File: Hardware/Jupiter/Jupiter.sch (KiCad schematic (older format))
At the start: 32 parts

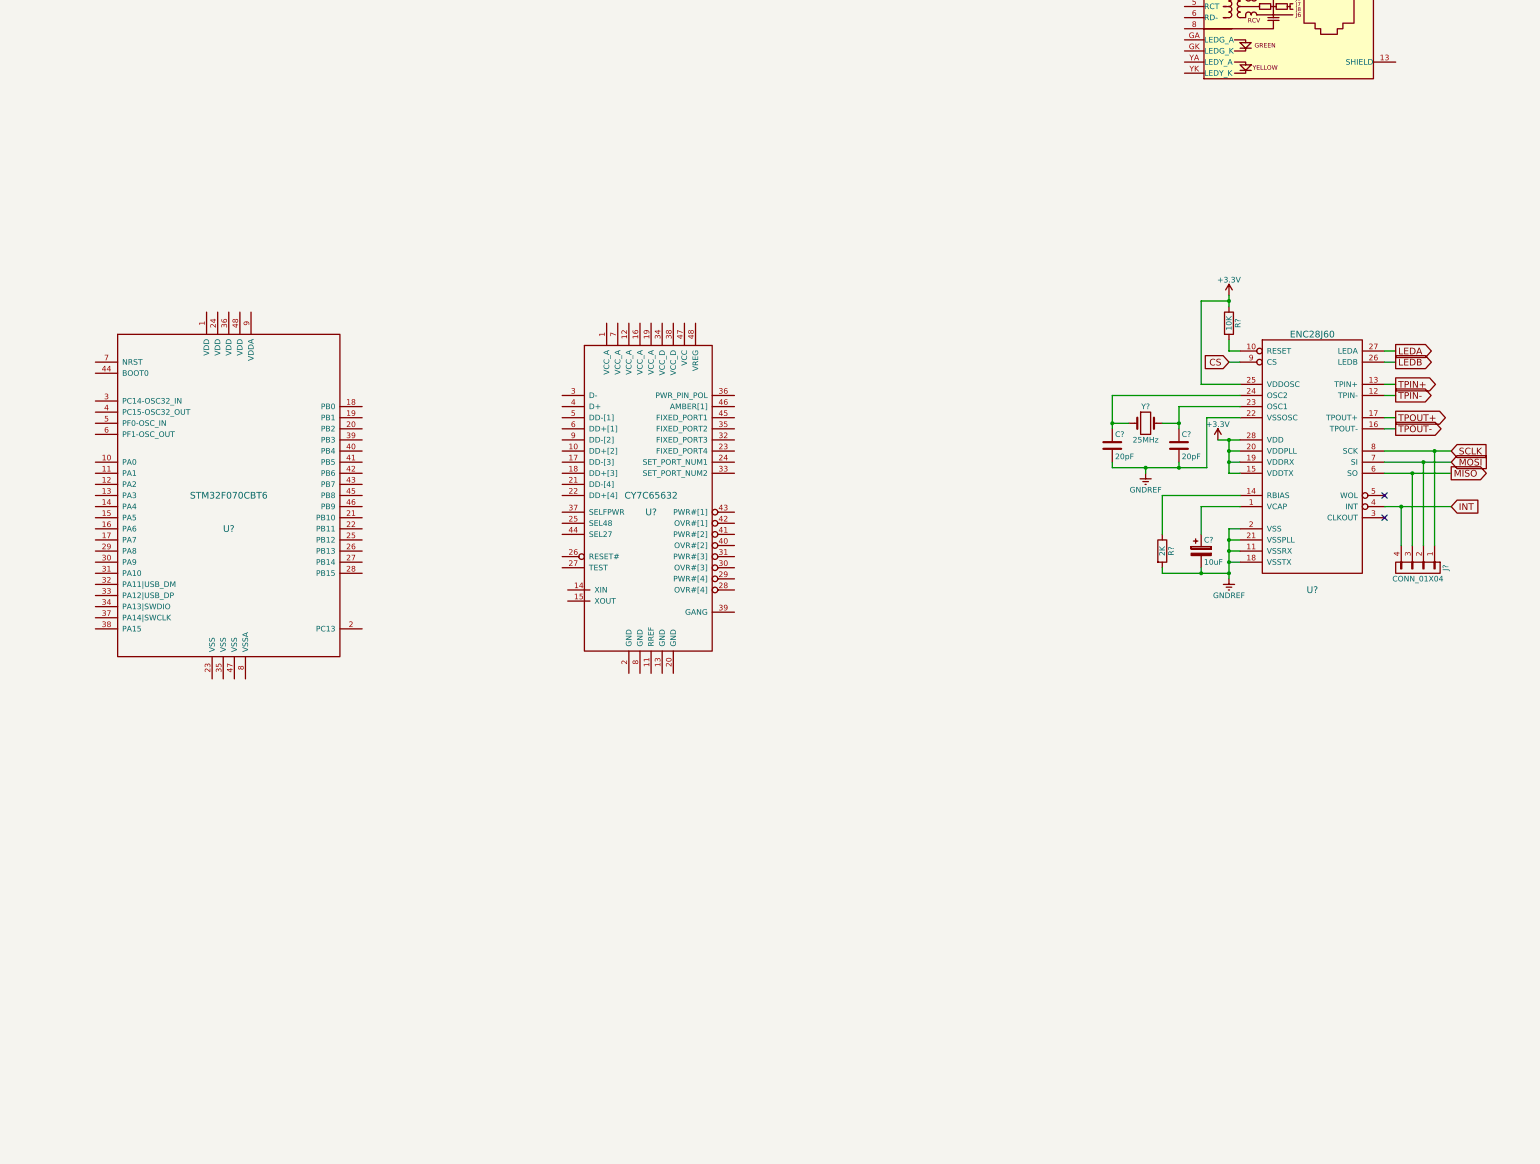
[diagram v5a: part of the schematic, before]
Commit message: USB additions.
1) Add external facing USB ports.
2) Add USB power control circuitry, cuts power to downstream USB in event of shorted pins (i.e., dodgey cabling).
3) Start filling out details for Cypress USB hub.
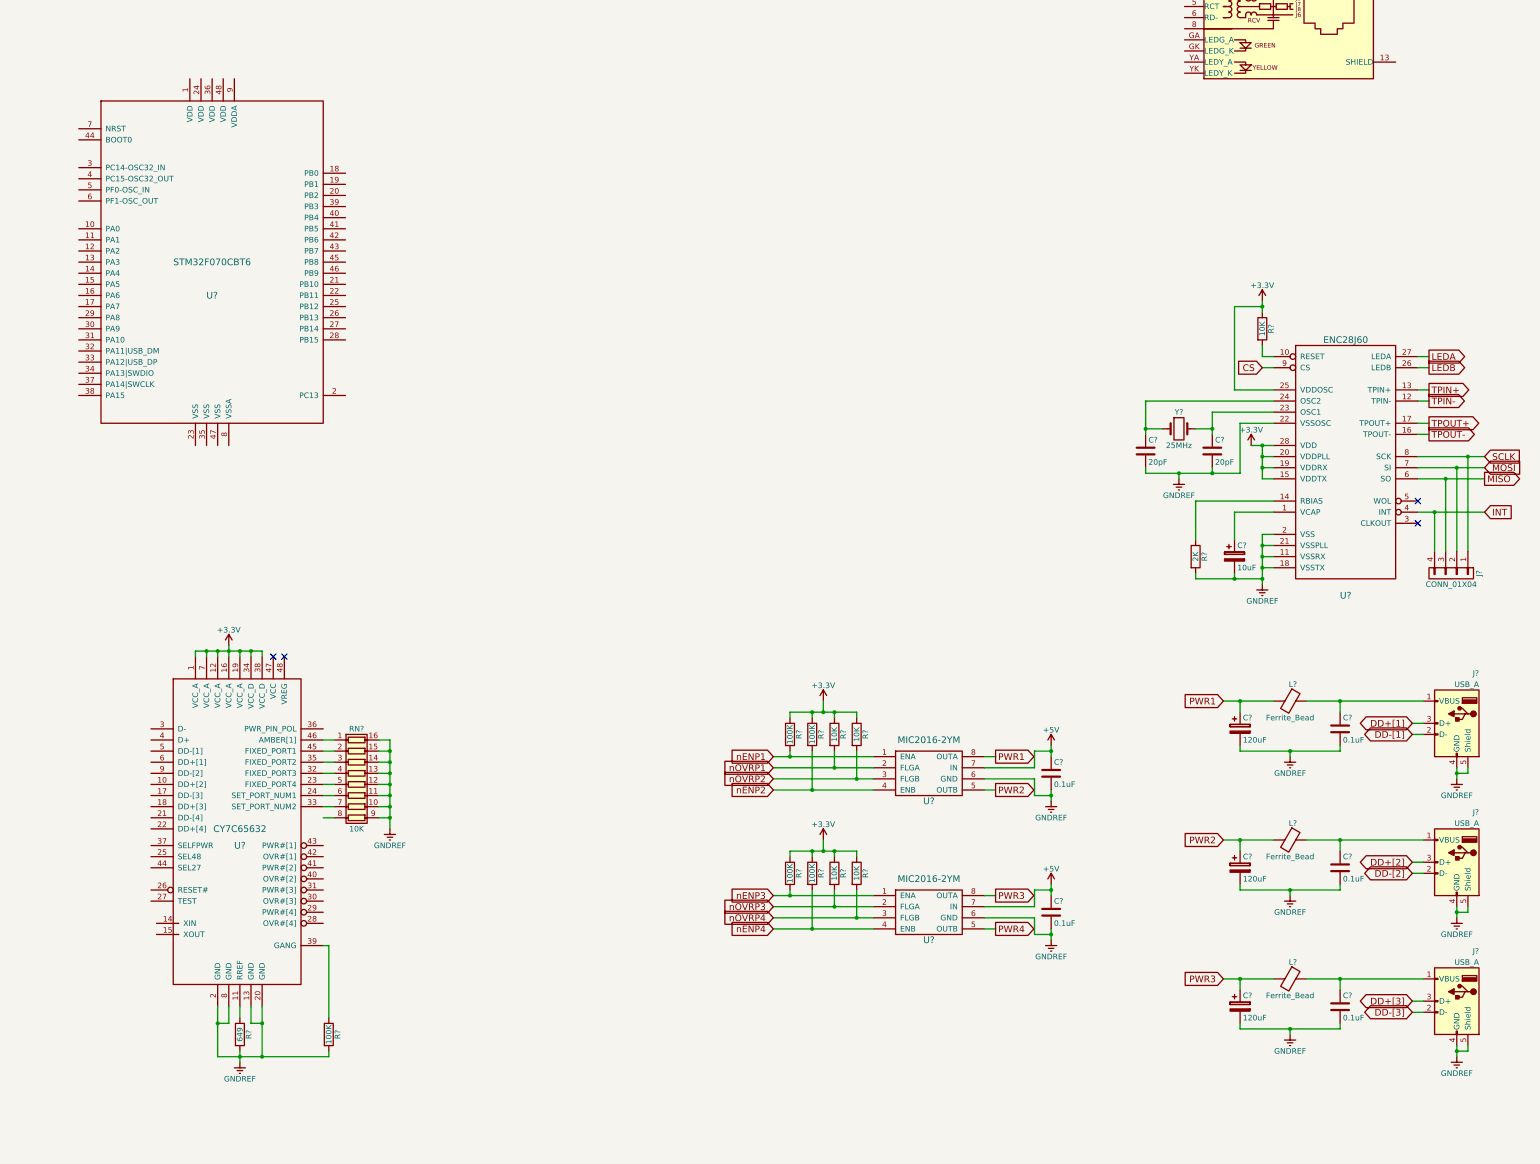
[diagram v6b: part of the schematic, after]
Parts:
- added C? (x5): 0.1uF, symbol C
- added C? (x3): 120uF, symbol CP
- added J? (x3): USB_A, symbol USB_A
- added L? (x3): Ferrite_Bead, symbol Ferrite_Bead
- added R? (x4): 10K, symbol R
- added R? (x5): 100K, symbol R
- added R?: 649, symbol R
- added RN?: 10K, symbol R_Pack08
- added U? (x2): MIC2016-2YM, symbol MIC2016-2YM
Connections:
- net +3V3: now also U?.1 (VCC_A), U?.12 (VCC_A), U?.16 (VCC_A), U?.19 (VCC_A), U?.34 (VCC_D), U?.38 (VCC_D), U?.7 (VCC_A), R?.1, R?.1, R?.1, R?.1, R?.1, R?.1, R?.1, R?.1
- net +5V: now also C?.1, C?.1, U?.7 (IN), U?.7 (IN)
- net GNDREF: now also U?.13 (GND), U?.2 (GND), U?.20 (GND), U?.8 (GND), C?.2, C?.2, C?.2, C?.2, C?.2, C?.2, C?.2, C?.2, J?.4 (GND), J?.4 (GND), J?.4 (GND), J?.5 (Shield), J?.5 (Shield), J?.5 (Shield), R?.2, R?.2, RN?.10 (R7.2), RN?.11 (R6.2), RN?.12 (R5.2), RN?.13 (R4.2), RN?.14 (R3.2), RN?.15 (R2.2), RN?.16 (R1.2), RN?.9 (R8.2), U?.6 (GND), U?.6 (GND)
- net at U?.11 (RREF): now also R?.1
- net at U?.23 (FIXED_PORT4): now also RN?.5 (R5.1)
- net at U?.24 (SET_PORT_NUM1): now also RN?.6 (R6.1)
- net at U?.32 (FIXED_PORT3): now also RN?.4 (R4.1)
- net at U?.33 (SET_PORT_NUM2): now also RN?.7 (R7.1)
- net at U?.35 (FIXED_PORT2): now also RN?.3 (R3.1)
- net at U?.39 (GANG): now also R?.1
- net at U?.45 (FIXED_PORT1): now also RN?.2 (R2.1)
- net at U?.46 (AMBER[1]): now also RN?.1 (R1.1)
- new net: C?.1, J?.1 (VBUS), L?.1 (x3)
- new net DD+[1]: J?.3 (D+)
- new net DD+[2]: J?.3 (D+)
- new net DD+[3]: J?.3 (D+)
- new net DD-[1]: J?.2 (D-)
- new net DD-[2]: J?.2 (D-)
- new net DD-[3]: J?.2 (D-)
- new net PWR1: C?.1, L?.2, U?.8 (OUTA)
- new net PWR2: C?.1, L?.2, U?.5 (OUTB)
- new net PWR3: C?.1, L?.2, U?.8 (OUTA)
- new net PWR4: U?.5 (OUTB)
- new net nENP1: R?.2, U?.1 (ENA)
- new net nENP2: R?.2, U?.4 (ENB)
- new net nENP3: R?.2, U?.1 (ENA)
- new net nENP4: R?.2, U?.4 (ENB)
- new net nOVRP1: R?.2, U?.2 (FLGA)
- new net nOVRP2: R?.2, U?.3 (FLGB)
- new net nOVRP3: R?.2, U?.2 (FLGA)
- new net nOVRP4: R?.2, U?.3 (FLGB)
- no-connect marks 3 -> 5
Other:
- moved on the sheet: C?, J?, R?, U?, Y?

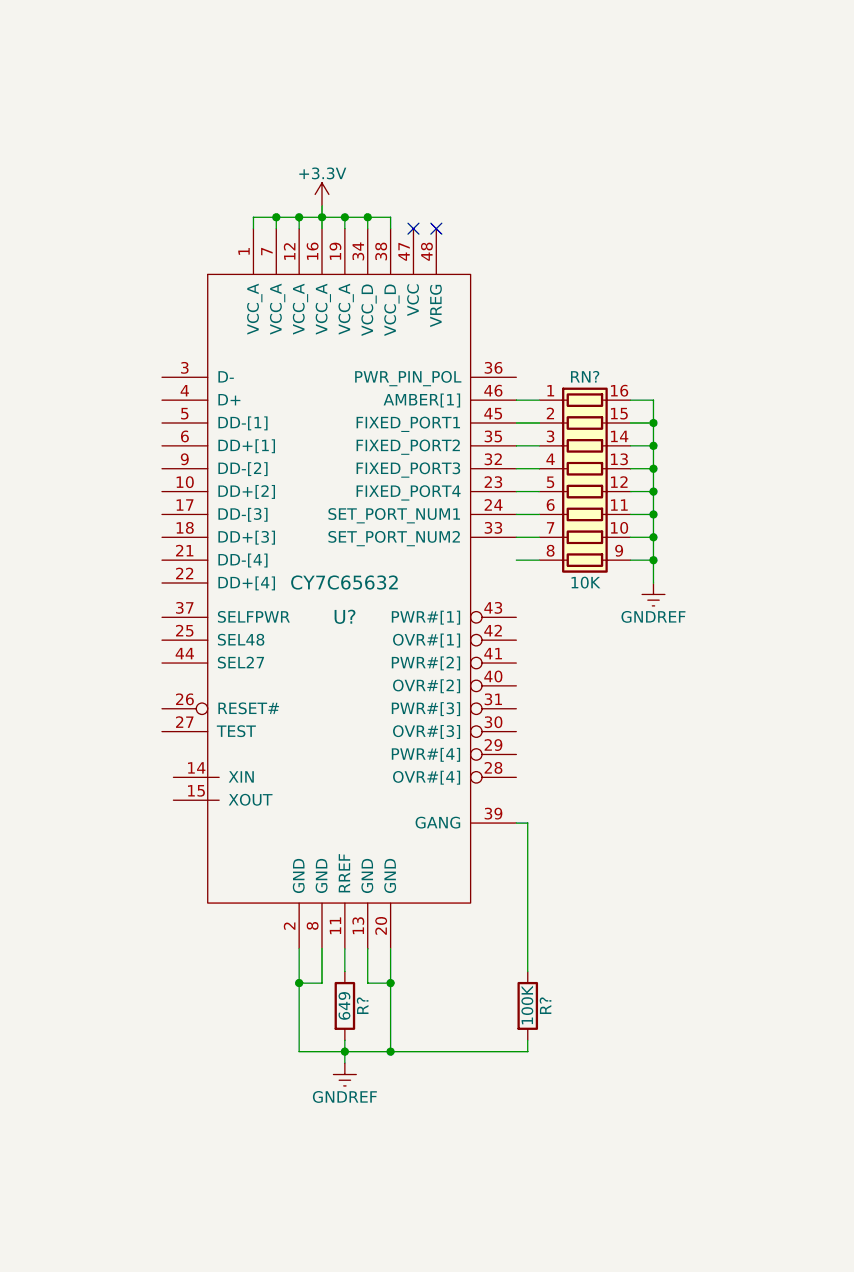
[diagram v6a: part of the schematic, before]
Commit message: Remove stale (and incorrect) Cypress USB hub part from MIC2026 library.
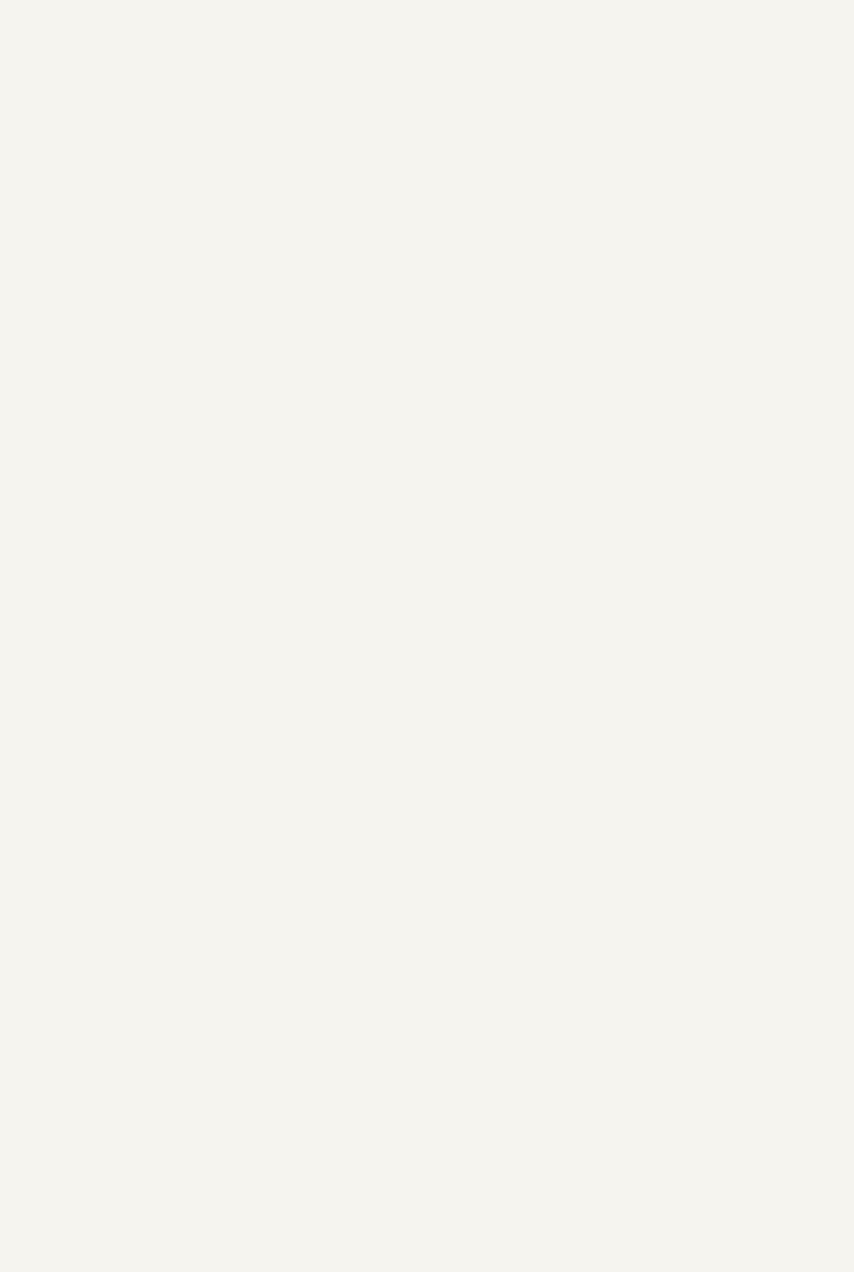
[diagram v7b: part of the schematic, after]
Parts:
- removed R?: 649, symbol R
- removed R?: 100K, symbol R
- removed RN?: 10K, symbol R_Pack08
- removed U?: CY7C65632, symbol CY7C65632
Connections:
- no-connect marks 5 -> 3
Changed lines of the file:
@@
-$EndComp
-$Comp
-L CY7C65632 U?
-U 1 1 5B60D432
-P 9000 11550
-F 0 "U?" H 9000 11400 60  0000 C CNN
-F 1 "CY7C65632" H 9000 11550 60  0000 C CNN
-F 2 "" H 9000 11550 60  0000 C CNN
-F 3 "" H 9000 11550 60  0000 C CNN
-	1    9000 11550
-	1    0    0    -1
 $EndComp
 $Comp
@@
 PWR3
 Connection ~ 18000 12900
-NoConn ~ 9300 10000
-NoConn ~ 9400 10000
-$Comp
-L +3.3V #PWR?
-U 1 1 5B6A8851
-P 8900 9900
-F 0 "#PWR?" H 8900 9750 50  0001 C CNN
-F 1 "+3.3V" H 8900 10040 50  0000 C CNN
-F 2 "" H 8900 9900 50  0001 C CNN
-F 3 "" H 8900 9900 50  0001 C CNN
-	1    8900 9900
-	1    0    0    -1
-$EndComp
-Wire Wire Line
-	8600 10000 8600 9950
-Wire Wire Line
-	8600 9950 9200 9950
-Wire Wire Line
-	9200 9950 9200 10000
-Wire Wire Line
-	9100 10000 9100 9950
-Connection ~ 9100 9950
-Wire Wire Line
-	9000 10000 9000 9950
-Connection ~ 9000 9950
-Wire Wire Line
-	8900 9900 8900 10000
-Connection ~ 8900 9950
-Wire Wire Line
-	8800 10000 8800 9950
-Connection ~ 8800 9950
-Wire Wire Line
-	8700 10000 8700 9950
-Connection ~ 8700 9950
-$Comp
-L R R?
-U 1 1 5B6A9578
-P 9000 13400
-F 0 "R?" V 9080 13400 50  0000 C CNN
-F 1 "649" V 9000 13400 50  0000 C CNN
-F 2 "" V 8930 13400 50  0001 C CNN
-F 3 "" H 9000 13400 50  0001 C CNN
-	1    9000 13400
-	1    0    0    -1
-$EndComp
-$Comp
-L GNDREF #PWR?
-U 1 1 5B6A9605
-P 9000 13650
-F 0 "#PWR?" H 9000 13400 50  0001 C CNN
-F 1 "GNDREF" H 9000 13500 50  0000 C CNN
-F 2 "" H 9000 13650 50  0001 C CNN
-F 3 "" H 9000 13650 50  0001 C CNN
-	1    9000 13650
-	1    0    0    -1
-$EndComp
-Wire Wire Line
-	9000 13650 9000 13550
-Wire Wire Line
-	9000 13250 9000 13150
-Wire Wire Line
-	8900 13150 8900 13300
-Wire Wire Line
-	8900 13300 8800 13300
-Wire Wire Line
-	8800 13150 8800 13600
-Wire Wire Line
-	8800 13600 9800 13600
-Connection ~ 9000 13600
-Connection ~ 8800 13300
-Wire Wire Line
-	9100 13150 9100 13300
-Wire Wire Line
-	9100 13300 9200 13300
-Wire Wire Line
-	9200 13600 9200 13150
-Connection ~ 9200 13300
-$Comp
-L R R?
-U 1 1 5B6AA592
-P 9800 13400
-F 0 "R?" V 9880 13400 50  0000 C CNN
-F 1 "100K" V 9800 13400 50  0000 C CNN
-F 2 "" V 9730 13400 50  0001 C CNN
-F 3 "" H 9800 13400 50  0001 C CNN
-	1    9800 13400
-	1    0    0    -1
-$EndComp
-Wire Wire Line
-	9800 13250 9800 12600
-Wire Wire Line
-	9800 12600 9750 12600
-Wire Wire Line
-	9800 13600 9800 13550
-Connection ~ 9200 13600
-$Comp
-L R_Pack08 RN?
-U 1 1 5B6AB122
-P 10050 11150
-F 0 "RN?" V 9550 11150 50  0000 C CNN
-F 1 "10K" V 10450 11150 50  0000 C CNN
-F 2 "" V 10525 11150 50  0001 C CNN
-F 3 "" H 10050 11150 50  0001 C CNN
-	1    10050 11150
-	0    1    1    0
-$EndComp
-Wire Wire Line
-	9850 10750 9750 10750
-Wire Wire Line
-	9750 10850 9850 10850
-Wire Wire Line
-	9850 10950 9750 10950
-Wire Wire Line
-	9750 11050 9850 11050
-Wire Wire Line
-	9850 11150 9750 11150
-Wire Wire Line
-	9750 11250 9850 11250
-Wire Wire Line
-	9850 11350 9750 11350
-Wire Wire Line
-	9750 11450 9850 11450
-$Comp
-L GNDREF #PWR?
-U 1 1 5B6AC07B
-P 10350 11550
-F 0 "#PWR?" H 10350 11300 50  0001 C CNN
-F 1 "GNDREF" H 10350 11400 50  0000 C CNN
-F 2 "" H 10350 11550 50  0001 C CNN
-F 3 "" H 10350 11550 50  0001 C CNN
-	1    10350 11550
-	1    0    0    -1
-$EndComp
-Wire Wire Line
-	10350 11550 10350 10750
-Wire Wire Line
-	10350 10750 10250 10750
-Wire Wire Line
-	10250 10850 10350 10850
-Connection ~ 10350 10850
-Wire Wire Line
-	10250 10950 10350 10950
-Connection ~ 10350 10950
-Wire Wire Line
-	10250 11050 10350 11050
-Connection ~ 10350 11050
-Wire Wire Line
-	10250 11150 10350 11150
-Connection ~ 10350 11150
-Wire Wire Line
-	10250 11250 10350 11250
-Connection ~ 10350 11250
-Wire Wire Line
-	10250 11350 10350 11350
-Connection ~ 10350 11350
-Wire Wire Line
-	10250 11450 10350 11450
-Connection ~ 10350 11450
 $EndSCHEMATC

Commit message: Finish USB subsection.
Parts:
- added C? (x2): C, symbol C
- added C?: 1uF, symbol C
- added R?: 649, symbol R
- added R?: 100K, symbol R
- added R?: 47K, symbol R
- added R?: 10K, symbol R
- added RN?: 10K, symbol R_Pack08
- added U?: CY7C65632, symbol CY7C65632
- added Y?: Crystal, symbol Crystal
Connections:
- net +3V3: now also R?.1, U?.1 (VCC_A), U?.12 (VCC_A), U?.16 (VCC_A), U?.19 (VCC_A), U?.25 (SEL48), U?.34 (VCC_D), U?.37 (SELFPWR), U?.38 (VCC_D), U?.44 (SEL27), U?.7 (VCC_A)
- net DD+[1]: now also U?.6 (DD+[1])
- net DD+[2]: now also U?.10 (DD+[2])
- net DD+[3]: now also U?.18 (DD+[3])
- net DD-[1]: now also U?.5 (DD-[1])
- net DD-[2]: now also U?.9 (DD-[2])
- net DD-[3]: now also U?.17 (DD-[3])
- net GNDREF: now also C?.2, C?.2, C?.2, R?.2, R?.2, R?.2, RN?.10 (R7.2), RN?.11 (R6.2), RN?.12 (R5.2), RN?.13 (R4.2), RN?.14 (R3.2), RN?.15 (R2.2), RN?.16 (R1.2), RN?.9 (R8.2), U?.13 (GND), U?.2 (GND), U?.20 (GND), U?.27 (TEST), U?.8 (GND)
- net nENP1: now also U?.43 (PWR#[1])
- net nENP2: now also U?.41 (PWR#[2])
- net nENP3: now also U?.31 (PWR#[3])
- net nENP4: now also U?.29 (PWR#[4])
- net nOVRP1: now also U?.42 (OVR#[1])
- net nOVRP2: now also U?.40 (OVR#[2])
- net nOVRP3: now also U?.30 (OVR#[3])
- net nOVRP4: now also U?.28 (OVR#[4])
- new net: R?.1, U?.11 (RREF)
- new net: C?.1, U?.14 (XIN), Y?.1
- new net: C?.1, U?.15 (XOUT), Y?.2
- new net: RN?.6 (R6.1), U?.23 (FIXED_PORT4)
- new net: RN?.7 (R7.1), U?.24 (SET_PORT_NUM1)
- new net: C?.1, R?.1, R?.2, U?.26 (RESET#)
- new net: RN?.5 (R5.1), U?.32 (FIXED_PORT3)
- new net: RN?.8 (R8.1), U?.33 (SET_PORT_NUM2)
- new net: RN?.4 (R4.1), U?.35 (FIXED_PORT2)
- new net: RN?.1 (R1.1), U?.36 (PWR_PIN_POL)
- new net: R?.1, U?.39 (GANG)
- new net: RN?.3 (R3.1), U?.45 (FIXED_PORT1)
- new net: RN?.2 (R2.1), U?.46 (AMBER[1])
- new net D+: U?.4 (D+)
- new net D-: U?.3 (D-)
- new net DD+[4]: U?.22 (DD+[4])
- new net DD-[4]: U?.21 (DD-[4])
- no-connect marks 3 -> 5
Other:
- moved on the sheet: C?, J?, L?, R?, U?
